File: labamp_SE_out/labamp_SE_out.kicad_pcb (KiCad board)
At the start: 2 copper layers, 55 x 26 mm, 13 parts, among them J1 Conn_02x06_Odd_Even, J2 Conn_02x06_Odd_Even, J3 Conn_01x03

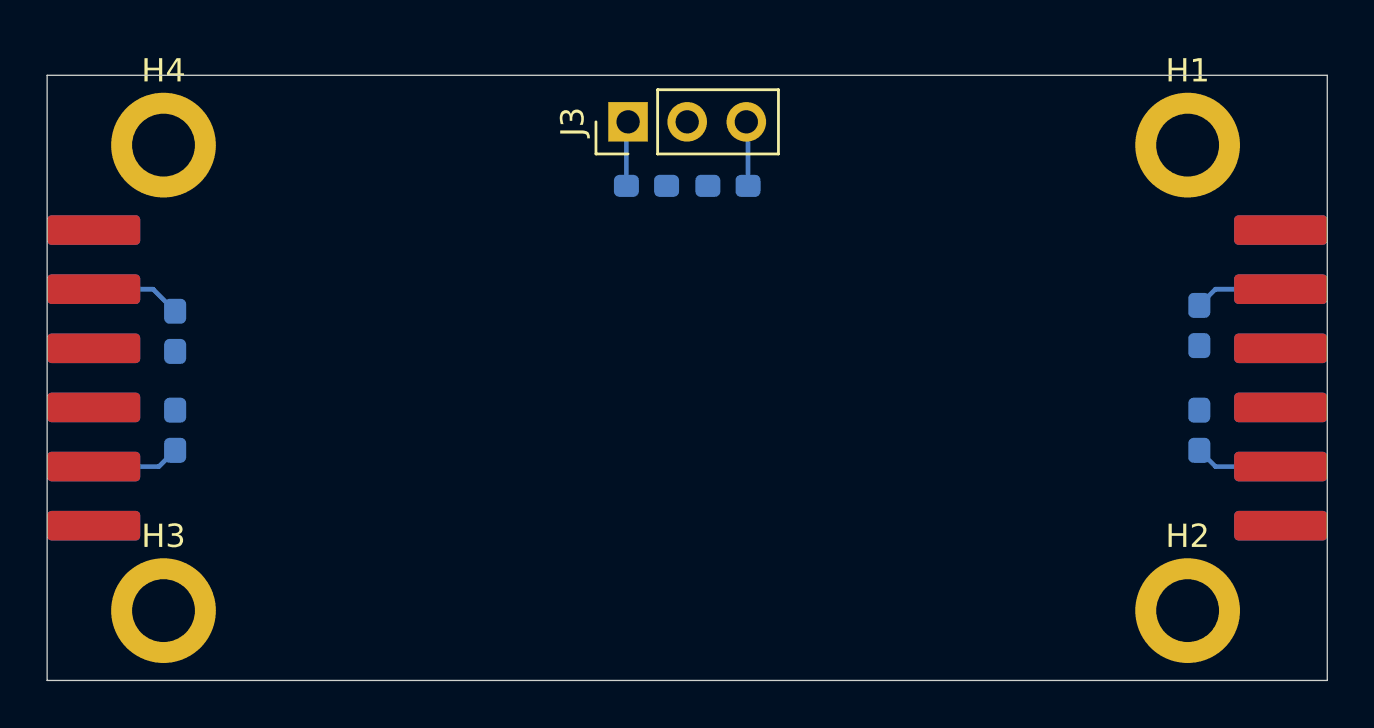
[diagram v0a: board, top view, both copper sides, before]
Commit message: Routed Single ended output PCB
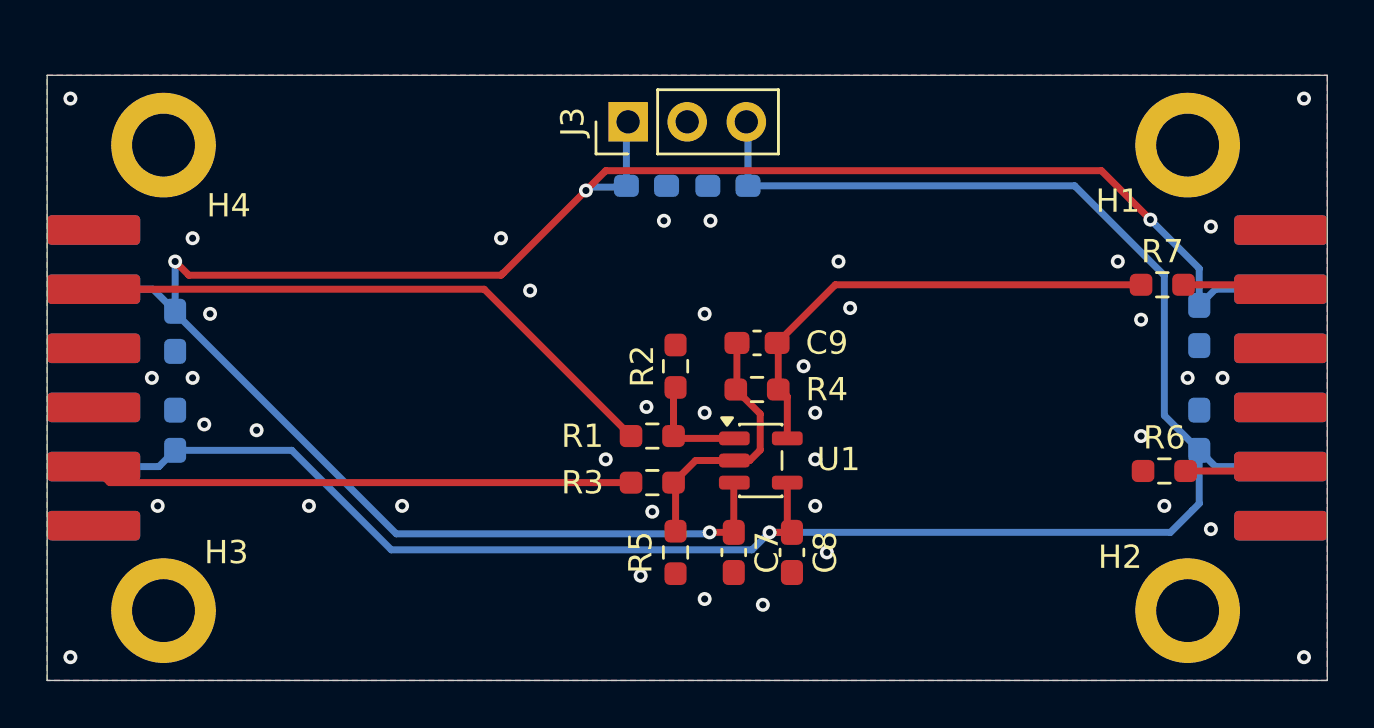
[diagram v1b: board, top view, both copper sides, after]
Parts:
- added C7: 100nF, Capacitor_SMD:C_0603_1608Metric_Pad1.08x0.95mm_HandSolder, F.Cu at (124.5, 97.5)
- added C8: 100nF, Capacitor_SMD:C_0603_1608Metric_Pad1.08x0.95mm_HandSolder, F.Cu at (127.0, 97.5)
- added C9: TBD, Capacitor_SMD:C_0603_1608Metric_Pad1.08x0.95mm_HandSolder, F.Cu at (125.5, 88.5)
- added R1: R, Resistor_SMD:R_0603_1608Metric_Pad0.98x0.95mm_HandSolder, F.Cu at (121.0, 92.5)
- added R2: R, Resistor_SMD:R_0603_1608Metric_Pad0.98x0.95mm_HandSolder, F.Cu at (122.0, 89.5)
- added R3: R, Resistor_SMD:R_0603_1608Metric_Pad0.98x0.95mm_HandSolder, F.Cu at (121.0, 94.5)
- added R4: R, Resistor_SMD:R_0603_1608Metric_Pad0.98x0.95mm_HandSolder, F.Cu at (125.5, 90.5)
- added R5: R, Resistor_SMD:R_0603_1608Metric_Pad0.98x0.95mm_HandSolder, F.Cu at (122.0, 97.5)
- added R6: R, Resistor_SMD:R_0603_1608Metric_Pad0.98x0.95mm_HandSolder, F.Cu at (143.0, 94.0)
- added R7: R, Resistor_SMD:R_0603_1608Metric_Pad0.98x0.95mm_HandSolder, F.Cu at (142.9, 86.0)
- added U1: ~, Package_TO_SOT_SMD:SOT-23-5, F.Cu at (125.7, 93.5)
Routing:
- net +3.3V: track 10.6 -> 94.0 mm, vias 0 -> 4
- net -3V3: track 10.6 -> 90.2 mm, vias 0 -> 1
- net /in+: track 0.00 -> 25.7 mm
- net /in-: track 0.00 -> 23.4 mm
- net Net-(C9-Pad2): track 0.00 -> 21.3 mm
- net Net-(U1--): track 0.00 -> 11.5 mm
- net Net-(U1-+): track 0.00 -> 4.78 mm
- net /out+: track 0.00 -> 4.25 mm
- net /out-: track 0.00 -> 4.17 mm
- net GND: vias 0 -> 40
- added copper zone on B.Cu, net GND
- added copper zone on F.Cu, net GND

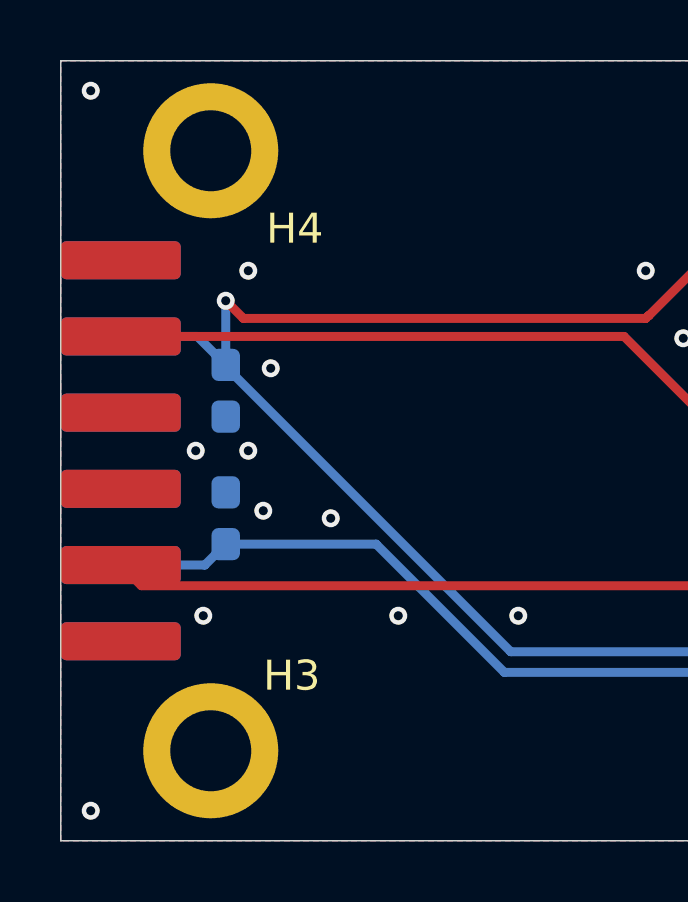
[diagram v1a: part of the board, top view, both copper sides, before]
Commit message: Moved mounting holes to avoid colision with header
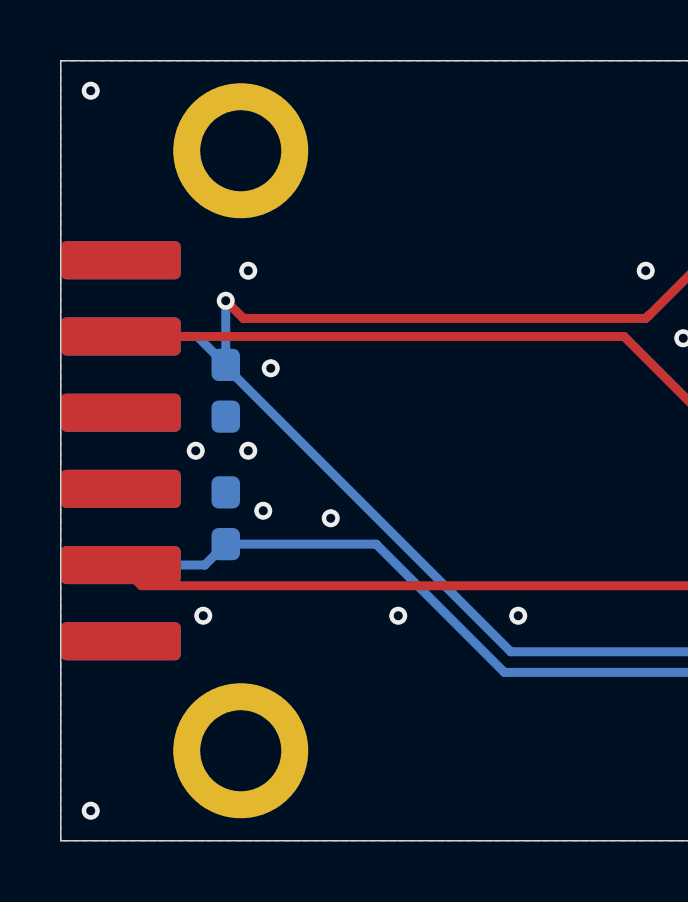
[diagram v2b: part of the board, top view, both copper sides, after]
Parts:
- moved H3 1.00 mm to (101.0, 100.0)
- moved H4 1.00 mm to (101.0, 80.0)
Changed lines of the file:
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@@
 	(footprint "MountingHole:MountingHole_2.7mm_M2.5_ISO14580_Pad"
 		(layer "F.Cu")
-		(at 100 80)
+		(at 101 80)
 		(descr "Mounting Hole 2.7mm, M2.5, generated by kicad-footprint-generator mountinghole.py")
 		(tags "mountinghole M2.5 ISO14580")
@@
 			(at 2.8 2.6 0)
 			(layer "F.SilkS")
+			(hide yes)
 			(effects
 				(font
@@
 	(footprint "MountingHole:MountingHole_2.7mm_M2.5_ISO14580_Pad"
 		(layer "F.Cu")
-		(at 100 100)
+		(at 101 100)
 		(descr "Mounting Hole 2.7mm, M2.5, generated by kicad-footprint-generator mountinghole.py")
 		(tags "mountinghole M2.5 ISO14580")
@@
 			(at 2.7 -2.5 0)
 			(layer "F.SilkS")
+			(hide yes)
 			(effects
 				(font

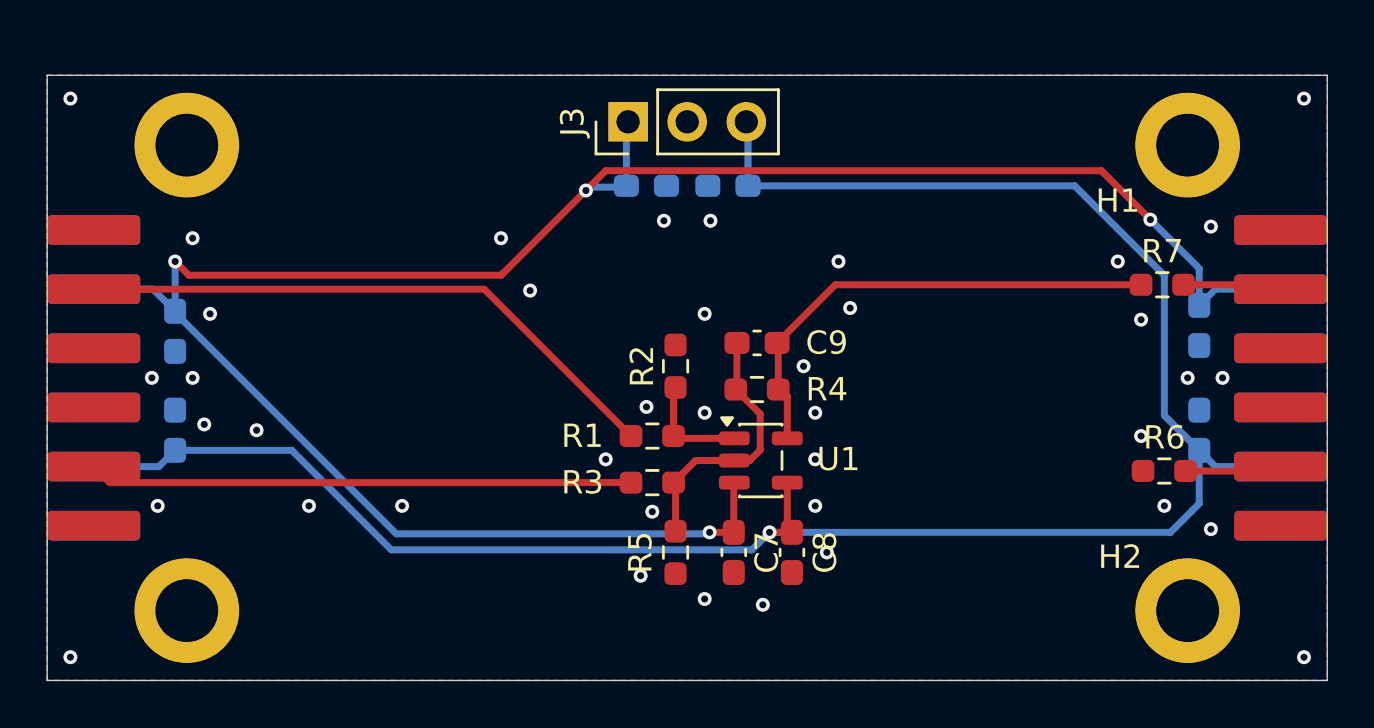
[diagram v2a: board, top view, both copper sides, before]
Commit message: Finished routing SE_out
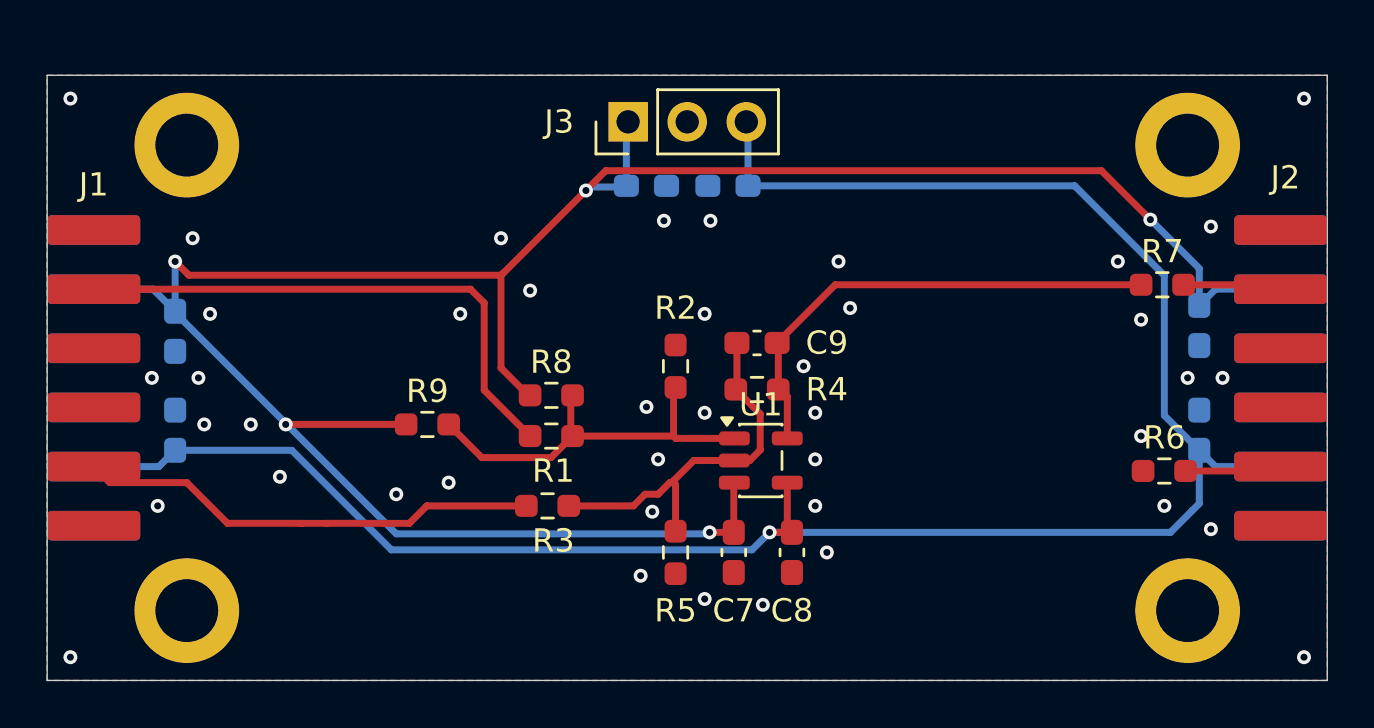
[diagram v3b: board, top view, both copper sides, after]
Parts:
- added R8: R, Resistor_SMD:R_0603_1608Metric_Pad0.98x0.95mm_HandSolder, F.Cu at (116.7, 90.8)
- added R9: R, Resistor_SMD:R_0603_1608Metric_Pad0.98x0.95mm_HandSolder, F.Cu at (111.3, 92.0)
- moved R3 4.61 mm to (116.5, 95.5)
- moved R1 4.34 mm to (116.7, 92.5)
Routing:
- net Net-(U1-+): track 4.78 -> 17.2 mm
- net +3.3V: track 94.0 -> 104.8 mm, vias 4 -> 5
- net Net-(U1--): track 11.5 -> 16.6 mm
- net /in-: track 23.4 -> 20.0 mm
- net /in+: track 25.7 -> 23.6 mm
- net GND: vias 40 -> 42

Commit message: Addedversion etc. in silkscreen
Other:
- board text added: "SE Ver 1.0 BHH"
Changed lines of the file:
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@@
 			(outputformat 1)
 			(mirror no)
-			(drillshape 1)
+			(drillshape 0)
 			(scaleselection 1)
-			(outputdirectory "")
+			(outputdirectory "labamp_SE_out_fab/")
 		)
 	)
@@
 		(layer "Edge.Cuts")
 	)
+	(gr_text "SE\nVer 1.0\nBHH"
+		(at 134.1 84.5 0)
+		(layer "F.SilkS")
+		(effects
+			(font
+				(size 1.5 1.5)
+				(thickness 0.3)
+				(bold yes)
+			)
+			(justify bottom)
+		)
+	)
 	(via
